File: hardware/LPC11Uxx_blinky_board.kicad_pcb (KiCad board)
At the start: 2 copper layers, 20 x 40 mm, 23 parts, among them J1 Conn_ARM_JTAG_SWD_10, J2 USB_B_Micro, J3 Conn_01x04_Male, SW1 SW_Push, U1 LPC11U37FBD48-401_, U2 MCP1825S, Y1 Crystal

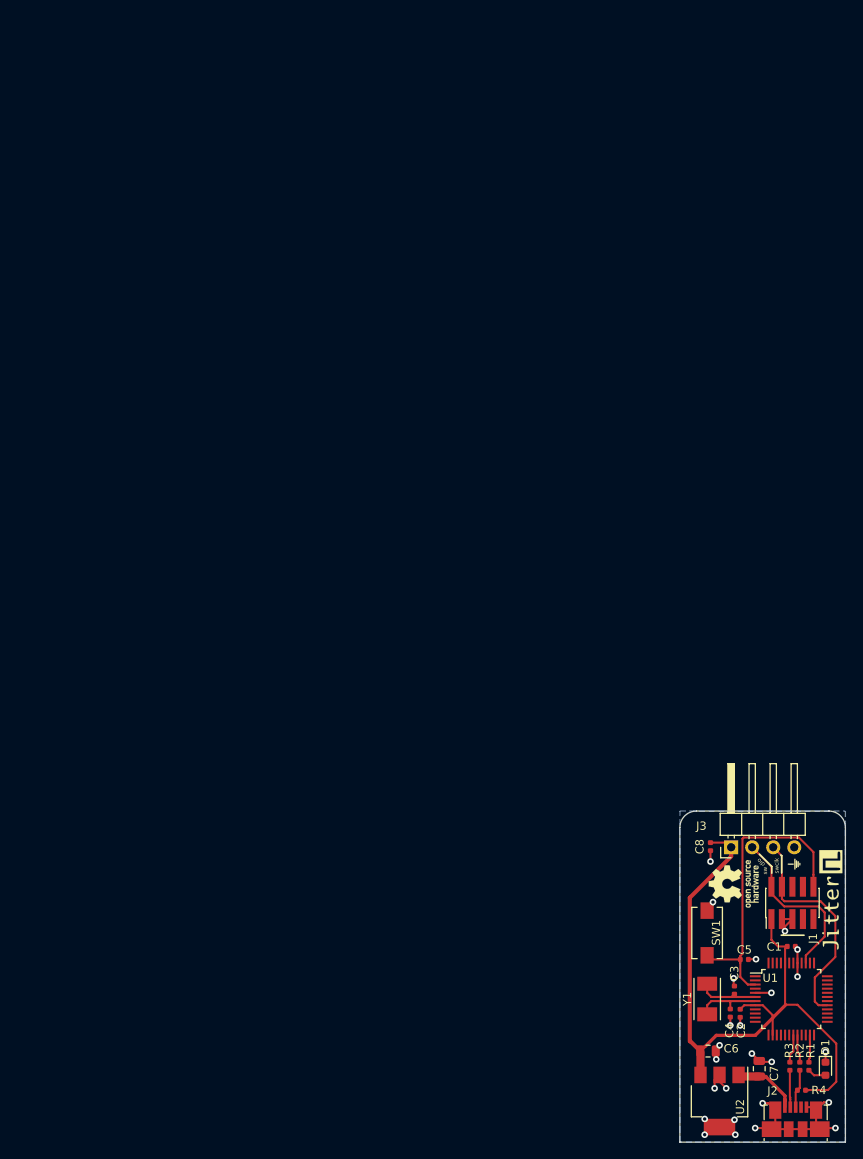
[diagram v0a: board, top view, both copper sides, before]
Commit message: Add frame with tooling holes and 4x LPC11 Blinkyboard.
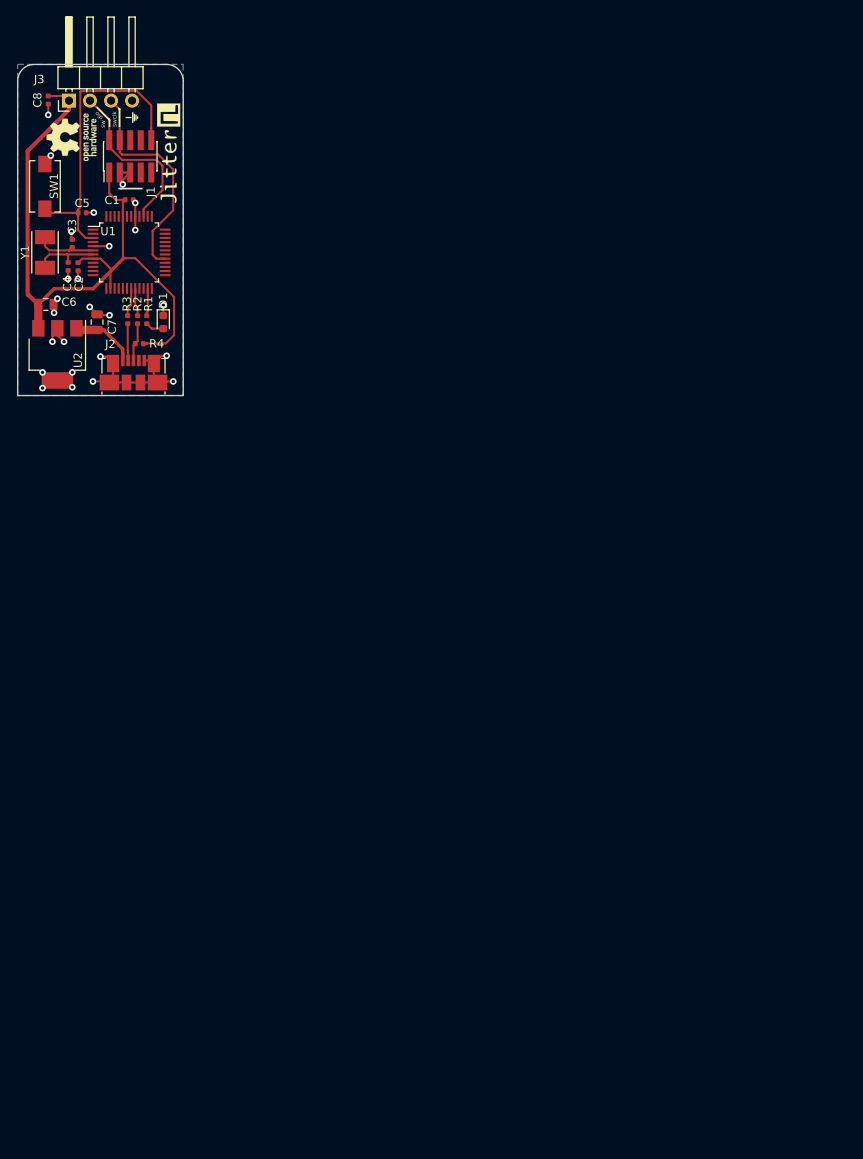
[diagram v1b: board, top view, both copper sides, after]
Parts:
- moved G*** 121.2 mm to (36.7, 48.7)
- moved C2 120.6 mm to (27.3, 44.2)
- moved C4 120.6 mm to (26.1, 44.2)
- moved C5 120.6 mm to (27.8, 37.7)
- moved C6 120.6 mm to (23.4, 48.8)
- moved G*** 120.6 mm to (38.2, 30.7)
- moved J2 120.6 mm to (34.0, 57.0)
- moved J3 120.6 mm to (26.2, 24.2)
- moved R1 120.6 mm to (35.6, 50.6)
- moved R2 120.6 mm to (34.5, 50.6)
- moved R3 120.6 mm to (33.3, 50.6)
- moved R4 120.6 mm to (34.7, 53.5)
- moved U1 120.6 mm to (33.5, 42.5)
- moved Y1 120.6 mm to (23.3, 42.5)
- moved C1 120.6 mm to (33.5, 36.2)
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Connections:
- C1 pad 1: (no net) -> +3V3
- C1 pad 2: (no net) -> GND
- C2 pad 1: (no net) -> +3V3
- C2 pad 2: (no net) -> GND
- C3 pad 1: (no net) -> GND
- C3 pad 2: (no net) -> Net-(C3-Pad2)
- C4 pad 1: (no net) -> GND
- C4 pad 2: (no net) -> Net-(C4-Pad2)
- C5 pad 1: (no net) -> /RESET
- C5 pad 2: (no net) -> GND
- C6 pad 1: (no net) -> GND
- C6 pad 2: (no net) -> +3V3
- C7 pad 1: (no net) -> GND
- C7 pad 2: (no net) -> +5V
- C8 pad 1: (no net) -> +3V3
- C8 pad 2: (no net) -> GND
- D1 pad 1: (no net) -> GND
- D1 pad 2: (no net) -> Net-(D1-Pad2)
- J1 pad 1: (no net) -> +3V3
- J1 pad 10: (no net) -> /RESET
- J1 pad 2: (no net) -> /SWDIO
- J1 pad 3: (no net) -> GND
- J1 pad 4: (no net) -> /SWCLK
- J1 pad 5: (no net) -> GND
- J1 pad 6: (no net) -> Net-(J1-Pad6)
- J1 pad 7: (no net) -> Net-(J1-Pad7)
- J1 pad 8: (no net) -> Net-(J1-Pad8)
- J1 pad 9: (no net) -> Net-(J1-Pad9)
- J2 pad 1: (no net) -> +5V
- J2 pad 2: (no net) -> /USBD-
- J2 pad 3: (no net) -> /USBD+
- J2 pad 4: (no net) -> Net-(J2-Pad4)
- J2 pad 5: (no net) -> GND
- J2 pad 6: (no net) -> GND
- J3 pad 1: (no net) -> +3V3
- J3 pad 2: (no net) -> /SWDIO
- J3 pad 3: (no net) -> /SWCLK
- J3 pad 4: (no net) -> GND
- R1 pad 1: (no net) -> Net-(R1-Pad1)
- R1 pad 2: (no net) -> Net-(D1-Pad2)
- R2 pad 1: (no net) -> /USBD+
- R2 pad 2: (no net) -> Net-(R2-Pad2)
- R3 pad 1: (no net) -> /USBD-
- R3 pad 2: (no net) -> Net-(R3-Pad2)
- R4 pad 1: (no net) -> /USBD+
- R4 pad 2: (no net) -> +3V3
- SW1 pad 1: (no net) -> /RESET
- SW1 pad 2: (no net) -> GND
- U1 pad 1: (no net) -> Net-(U1-Pad1)
- U1 pad 10: (no net) -> Net-(U1-Pad10)
- U1 pad 11: (no net) -> Net-(U1-Pad11)
- U1 pad 12: (no net) -> Net-(U1-Pad12)
- U1 pad 13: (no net) -> Net-(U1-Pad13)
- U1 pad 14: (no net) -> +3V3
- U1 pad 15: (no net) -> Net-(U1-Pad15)
- U1 pad 16: (no net) -> Net-(U1-Pad16)
- U1 pad 17: (no net) -> Net-(U1-Pad17)
- U1 pad 18: (no net) -> Net-(U1-Pad18)
- U1 pad 19: (no net) -> Net-(R3-Pad2)
- U1 pad 2: (no net) -> Net-(U1-Pad2)
- U1 pad 20: (no net) -> Net-(R2-Pad2)
- U1 pad 21: (no net) -> Net-(U1-Pad21)
- U1 pad 22: (no net) -> Net-(U1-Pad22)
- U1 pad 23: (no net) -> Net-(R1-Pad1)
- U1 pad 24: (no net) -> Net-(U1-Pad24)
- U1 pad 25: (no net) -> Net-(U1-Pad25)
- U1 pad 26: (no net) -> Net-(U1-Pad26)
- U1 pad 27: (no net) -> Net-(U1-Pad27)
- U1 pad 28: (no net) -> Net-(U1-Pad28)
- U1 pad 29: (no net) -> /SWCLK
- U1 pad 3: (no net) -> /RESET
- U1 pad 30: (no net) -> Net-(U1-Pad30)
- U1 pad 31: (no net) -> Net-(U1-Pad31)
- U1 pad 32: (no net) -> Net-(U1-Pad32)
- U1 pad 33: (no net) -> Net-(U1-Pad33)
- U1 pad 34: (no net) -> Net-(U1-Pad34)
- U1 pad 35: (no net) -> Net-(U1-Pad35)
- U1 pad 36: (no net) -> Net-(U1-Pad36)
- U1 pad 37: (no net) -> Net-(U1-Pad37)
- U1 pad 38: (no net) -> Net-(U1-Pad38)
- U1 pad 39: (no net) -> /SWDIO
- U1 pad 4: (no net) -> Net-(U1-Pad4)
- U1 pad 40: (no net) -> Net-(U1-Pad40)
- U1 pad 41: (no net) -> GND
- U1 pad 42: (no net) -> Net-(U1-Pad42)
- U1 pad 43: (no net) -> Net-(U1-Pad43)
- U1 pad 44: (no net) -> +3V3
- U1 pad 45: (no net) -> Net-(U1-Pad45)
- U1 pad 46: (no net) -> Net-(U1-Pad46)
- U1 pad 47: (no net) -> Net-(U1-Pad47)
- U1 pad 48: (no net) -> Net-(U1-Pad48)
- U1 pad 5: (no net) -> GND
- U1 pad 6: (no net) -> Net-(C3-Pad2)
- U1 pad 7: (no net) -> Net-(C4-Pad2)
- U1 pad 8: (no net) -> +3V3
- U1 pad 9: (no net) -> Net-(U1-Pad9)
- U2 pad 1: (no net) -> +5V
- U2 pad 2: (no net) -> GND
- U2 pad 3: (no net) -> +3V3
- Y1 pad 1: (no net) -> Net-(C3-Pad2)
- Y1 pad 2: (no net) -> Net-(C4-Pad2)
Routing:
- net (no net): track 259.1 -> 0.00 mm, vias 25 -> 0
- net +3V3: track 0.00 -> 81.9 mm
- net GND: track 0.00 -> 46.6 mm, vias 0 -> 25
- net /RESET: track 0.00 -> 36.8 mm
- net /SWCLK: track 0.00 -> 27.0 mm
- net /SWDIO: track 0.00 -> 21.0 mm
- net +5V: track 0.00 -> 8.25 mm
- net Net-(C4-Pad2): track 0.00 -> 8.11 mm
- net Net-(C3-Pad2): track 0.00 -> 7.66 mm
- net /USBD+: track 0.00 -> 4.66 mm
- net /USBD-: track 0.00 -> 4.55 mm
- net Net-(R3-Pad2): track 0.00 -> 3.46 mm
- net Net-(R2-Pad2): track 0.00 -> 3.40 mm
- net Net-(R1-Pad1): track 0.00 -> 3.33 mm
- net Net-(D1-Pad2): track 0.00 -> 2.26 mm
- added copper zone on B.Cu, net GND
- removed copper zone on B.Cu, net (none)

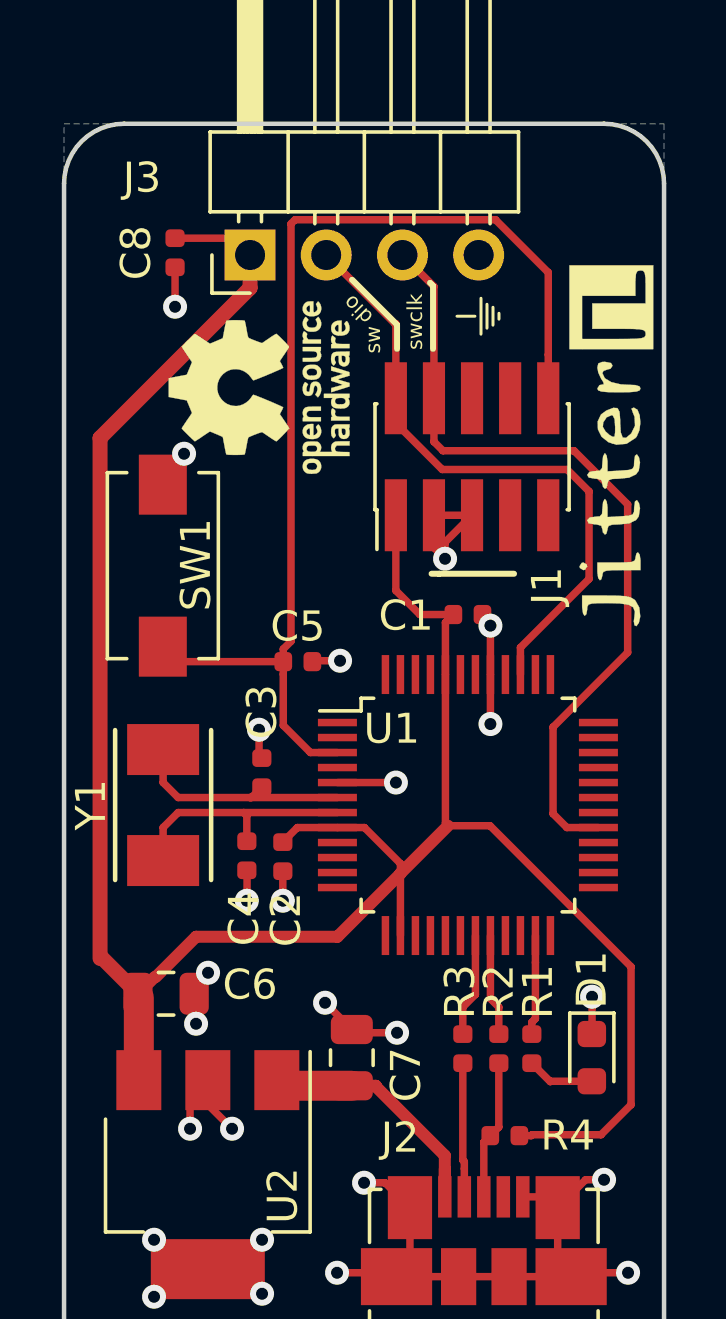
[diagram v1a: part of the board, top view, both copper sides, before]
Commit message: Use crystal symbol from our library
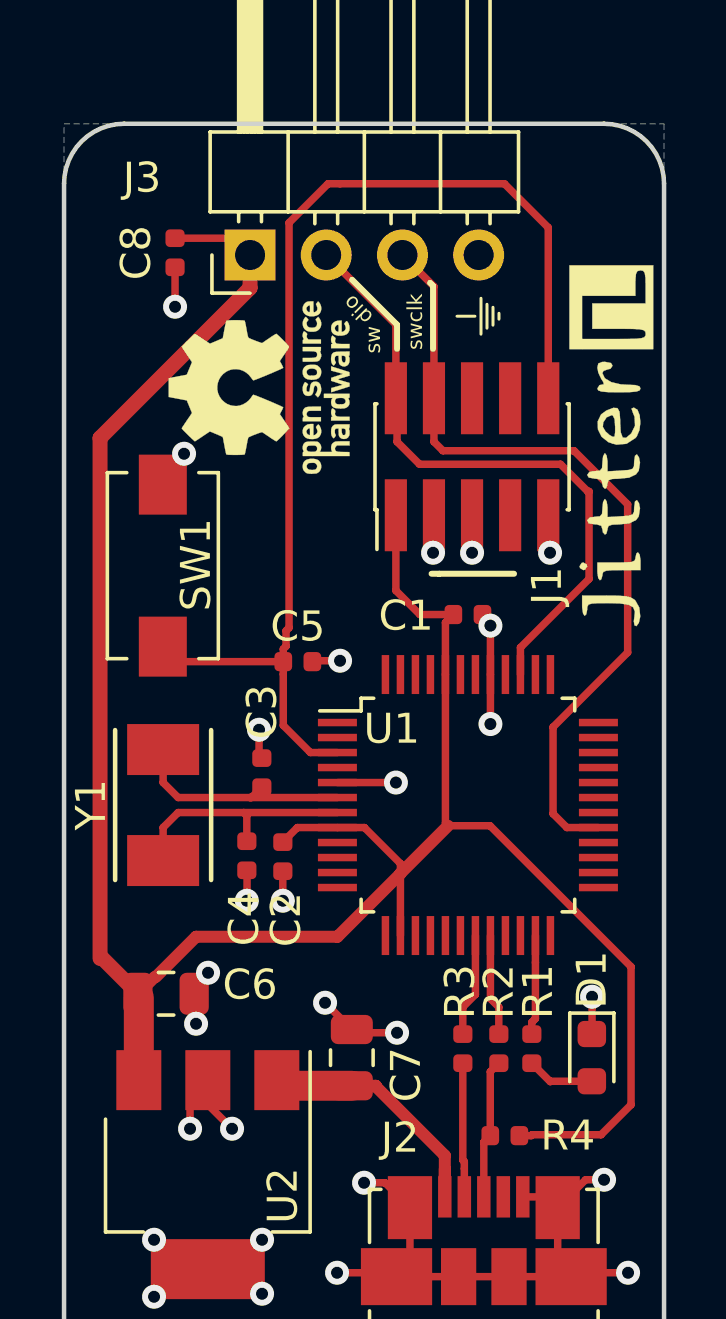
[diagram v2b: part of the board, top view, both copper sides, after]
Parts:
- Y1: footprint Crystal:Crystal_SMD_TXC_7A-2Pin_5.0x3.2mm -> Jitter_Footprints:Crystal_SMD_TXC_7A-2Pin_5.0x3.2mm
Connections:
- J1 pad 9: Net-(J1-Pad9) -> GND
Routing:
- net /RESET: track 36.8 -> 38.7 mm
- net /SWDIO: track 21.0 -> 22.2 mm
- net GND: track 46.6 -> 45.7 mm, vias 25 -> 27
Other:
- rule pad_to_mask_clearance: 0.2 -> 0.075

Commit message: PCB layout: minor adjustments
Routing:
- net +3V3: track 81.9 -> 82.7 mm
- net +5V: track 8.25 -> 8.97 mm
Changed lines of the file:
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@@
-(kicad_pcb (version 20171130) (host pcbnew "(5.0.1-3-g963ef8bb5)")
+(kicad_pcb (version 20171130) (host pcbnew 5.0.1-33cea8e~68~ubuntu18.04.1)
   (general
     (thickness 1.6)
     (drawings 35)
-    (tracks 194)
+    (tracks 188)
     (zones 0)
     (modules 23)
@@
     (34 B.Paste user hide)
     (35 F.Paste user hide)
-    (36 B.SilkS user hide)
-    (37 F.SilkS user hide)
+    (36 B.SilkS user)
+    (37 F.SilkS user)
     (38 B.Mask user hide)
     (39 F.Mask user)
@@
   (via (at 33.6 34.1) (size 0.8) (drill 0.4) (layers F.Cu B.Cu) (net 1))
   (segment (start 33.6 32.85) (end 33.6 34.1) (width 0.25) (layer F.Cu) (net 1))
-  (segment (start 29.112498 46.9) (end 31.212498 44.8) (width 0.4) (layer F.Cu) (net 2))
   (segment (start 22.492498 48.929998) (end 22.3625 48.8) (width 0.25) (layer F.Cu) (net 2))
   (segment (start 35.177498 53.530002) (end 35.572498 53.530002) (width 0.25) (layer F.Cu) (net 2))
@@
   (segment (start 31.860002 36.160002) (end 32.977498 36.160002) (width 0.25) (layer F.Cu) (net 2))
   (segment (start 31.212498 44.8) (end 31.212498 46.860002) (width 0.25) (layer F.Cu) (net 2))
-  (segment (start 23.056237 48.243763) (end 24.4 46.9) (width 0.4) (layer F.Cu) (net 2))
-  (segment (start 24.4 46.9) (end 29.112498 46.9) (width 0.4) (layer F.Cu) (net 2))
   (segment (start 22.4625 48.8) (end 23.018737 48.243763) (width 0.4) (layer F.Cu) (net 2))
   (segment (start 23.018737 48.243763) (end 23.056237 48.243763) (width 0.25) (layer F.Cu) (net 2))
-  (segment (start 22.492498 51.680002) (end 22.492498 48.929998) (width 1) (layer F.Cu) (net 2))
+  (segment (start 22.45 51.700004) (end 22.45 48.95) (width 1) (layer F.Cu) (net 2))
   (segment (start 38.9 47.9) (end 34.2 43.2) (width 0.25) (layer F.Cu) (net 2))
   (segment (start 34.2 43.2) (end 32.8 43.2) (width 0.25) (layer F.Cu) (net 2))
@@
   (segment (start 21.287504 47.625004) (end 22.4625 48.8) (width 0.5) (layer F.Cu) (net 2))
   (segment (start 26.2 25.275) (end 21.2 30.275) (width 0.5) (layer F.Cu) (net 2))
-  (segment (start 21.2 30.275) (end 21.2 47.625004) (width 0.5) (layer F.Cu) (net 2) (status 40000))
   (segment (start 31.06 35.36) (end 31.860002 36.160002) (width 0.25) (layer F.Cu) (net 2))
   (segment (start 31.06 32.85) (end 31.06 35.36) (width 0.25) (layer F.Cu) (net 2))
@@
   (segment (start 30.012498 43.260002) (end 31.212498 44.460002) (width 0.25) (layer F.Cu) (net 2))
   (segment (start 31.212498 44.460002) (end 31.212498 44.8) (width 0.25) (layer F.Cu) (net 2))
+  (segment (start 21.25 30.199996) (end 21.25 47.55) (width 0.5) (layer F.Cu) (net 2) (status 40000))
+  (segment (start 24.3625 46.9) (end 22.4625 48.8) (width 0.4) (layer F.Cu) (net 2))
+  (segment (start 31.212498 44.8) (end 29.112498 46.9) (width 0.4) (layer F.Cu) (net 2))
+  (segment (start 29.112498 46.9) (end 24.3625 46.9) (width 0.4) (layer F.Cu) (net 2))
   (segment (start 26.247498 42.260002) (end 26.192498 42.260002) (width 0.25) (layer F.Cu) (net 3))
   (segment (start 29.112498 42.260002) (end 26.192498 42.260002) (width 0.25) (layer F.Cu) (net 3))
@@
   (segment (start 28.212498 40.760002) (end 27.307498 39.855002) (width 0.25) (layer F.Cu) (net 5))
   (segment (start 27.307498 37.730002) (end 23.792498 37.730002) (width 0.25) (layer F.Cu) (net 5))
+  (segment (start 36.14 23.26) (end 34.68 21.8) (width 0.25) (layer F.Cu) (net 5))
+  (segment (start 28.8 21.8) (end 27.5 23.1) (width 0.25) (layer F.Cu) (net 5))
   (segment (start 36.14 28.95) (end 36.14 23.26) (width 0.25) (layer F.Cu) (net 5))
-  (segment (start 36.14 23.26) (end 34.68 21.8) (width 0.25) (layer F.Cu) (net 5))
-  (segment (start 34.68 21.8) (end 29.2 21.8) (width 0.25) (layer F.Cu) (net 5))
-  (segment (start 28.8 21.8) (end 29.2 21.8) (width 0.25) (layer F.Cu) (net 5))
-  (segment (start 27.5 23.1) (end 28.8 21.8) (width 0.25) (layer F.Cu) (net 5))
-  (segment (start 27.4 36.7) (end 27.5 36.6) (width 0.25) (layer F.Cu) (net 5))
-  (segment (start 27.5 36.6) (end 27.5 23.1) (width 0.25) (layer F.Cu) (net 5))
-  (segment (start 27.4 37.2175) (end 27.4 36.7) (width 0.25) (layer F.Cu) (net 5))
-  (segment (start 27.307498 37.310002) (end 27.4 37.2175) (width 0.25) (layer F.Cu) (net 5))
-  (segment (start 27.307498 37.730002) (end 27.307498 37.310002) (width 0.25) (layer F.Cu) (net 5))
+  (segment (start 34.68 21.8) (end 28.8 21.8) (width 0.25) (layer F.Cu) (net 5))
+  (segment (start 27.307498 37.492502) (end 27.307498 37.730002) (width 0.25) (layer F.Cu) (net 5))
+  (segment (start 27.5 23.1) (end 27.5 37.3) (width 0.25) (layer F.Cu) (net 5))
+  (segment (start 27.5 37.3) (end 27.307498 37.492502) (width 0.25) (layer F.Cu) (net 5))
   (segment (start 27.279998 51.867502) (end 27.092498 51.680002) (width 0.25) (layer F.Cu) (net 6))
-  (segment (start 30.392498 51.867502) (end 30.392498 51.892498) (width 0.4) (layer F.Cu) (net 6))
   (segment (start 32.692498 55.570002) (end 32.692498 54.85) (width 0.4) (layer F.Cu) (net 6))
   (segment (start 32.692498 54.85) (end 32.692498 54.630002) (width 0.4) (layer F.Cu) (net 6))
-  (segment (start 30.392498 51.892498) (end 32.692498 54.192498) (width 0.4) (layer F.Cu) (net 6))
   (segment (start 29.592498 51.867502) (end 27.279998 51.867502) (width 1) (layer F.Cu) (net 6))
+  (segment (start 32.692498 54.480002) (end 32.692498 55.570002) (width 0.4) (layer F.Cu) (net 6))
+  (segment (start 32.692498 54.167502) (end 32.692498 54.480002) (width 0.4) (layer F.Cu) (net 6))
+  (segment (start 30.392498 51.867502) (end 32.692498 54.167502) (width 0.4) (layer F.Cu) (net 6))
   (segment (start 29.592498 51.867502) (end 30.392498 51.867502) (width 0.4) (layer F.Cu) (net 6))
-  (segment (start 32.692498 54.192498) (end 32.692498 54.85) (width 0.4) (layer F.Cu) (net 6))
   (segment (start 36.207498 51.730002) (end 36.219998 51.717502) (width 0.25) (layer F.Cu) (net 7))
   (segment (start 36.219998 51.717502) (end 37.592498 51.717502) (width 0.25) (layer F.Cu) (net 7))
@@
   (segment (start 34.207498 51.400002) (end 34.492498 51.115002) (width 0.25) (layer F.Cu) (net 14))
   (segment (start 34.207498 53.530002) (end 34.207498 51.400002) (width 0.25) (layer F.Cu) (net 14))
-  (segment (start 33.292498 51.115002) (end 33.292498 54.346106) (width 0.25) (layer F.Cu) (net 15))
-  (segment (start 33.342498 54.396106) (end 33.342498 54.630002) (width 0.25) (layer F.Cu) (net 15))
-  (segment (start 33.342498 54.630002) (end 33.342498 55.570002) (width 0.25) (layer F.Cu) (net 15))
   (segment (start 33.342498 51.165002) (end 33.292498 51.115002) (width 0.25) (layer F.Cu) (net 15))
-  (segment (start 33.292498 54.346106) (end 33.342498 54.396106) (width 0.25) (layer F.Cu) (net 15))
+  (segment (start 33.342498 51.165002) (end 33.342498 55.570002) (width 0.25) (layer F.Cu) (net 15))
   (segment (start 35.592498 50.145002) (end 35.592498 49.750002) (width 0.25) (layer F.Cu) (net 16))
   (segment (start 35.712498 47.760002) (end 35.712498 46.860002) (width 0.25) (layer F.Cu) (net 16))
@@
     (connect_pads (clearance 0.508))
     (min_thickness 0.254)
-    (fill yes (arc_segments 16) (thermal_gap 0.508) (thermal_bridge_width 0.508))
+    (fill yes (arc_segments 32) (thermal_gap 0.508) (thermal_bridge_width 0.508))
     (polygon
       (pts
